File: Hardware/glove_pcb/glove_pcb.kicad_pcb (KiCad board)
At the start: 4 copper layers, 144.6 x 80.7 mm, 124 parts, among them J1 OSTVN02A150, J2 OSTVN02A150, J3 54-00130, J4 0430451000, J5 302-R141, J6 302-R141, J7 61300611121, J8 67997-206HLF, J9 22053061, M1 MountingHole_3.5mm_Pad, M2 MountingHole_3.5mm_Pad, M3 MountingHole_3.5mm_Pad, M4 MountingHole_3.5mm_Pad, U1 AP63205WU, U10 BZA408B, U11 BZA408B, U12 MCP3008, U13 ATmega328PB-A, U14 MCP3008, U15 MCP3008, U16 BM70BLES1FC2-0B04AA, U17 MCP111T-195I/TT, U18 74LVC1T45GW_125, U19 74LVC1T45GW_125, U2 TCR2EF33_LMCT, U3 DRV8876PWPR, U4 DRV8876PWPR, U5 DRV8876PWPR, U6 DRV8876PWPR, U7 DRV8876PWPR, U8 BZA408B, U9 BZA408B

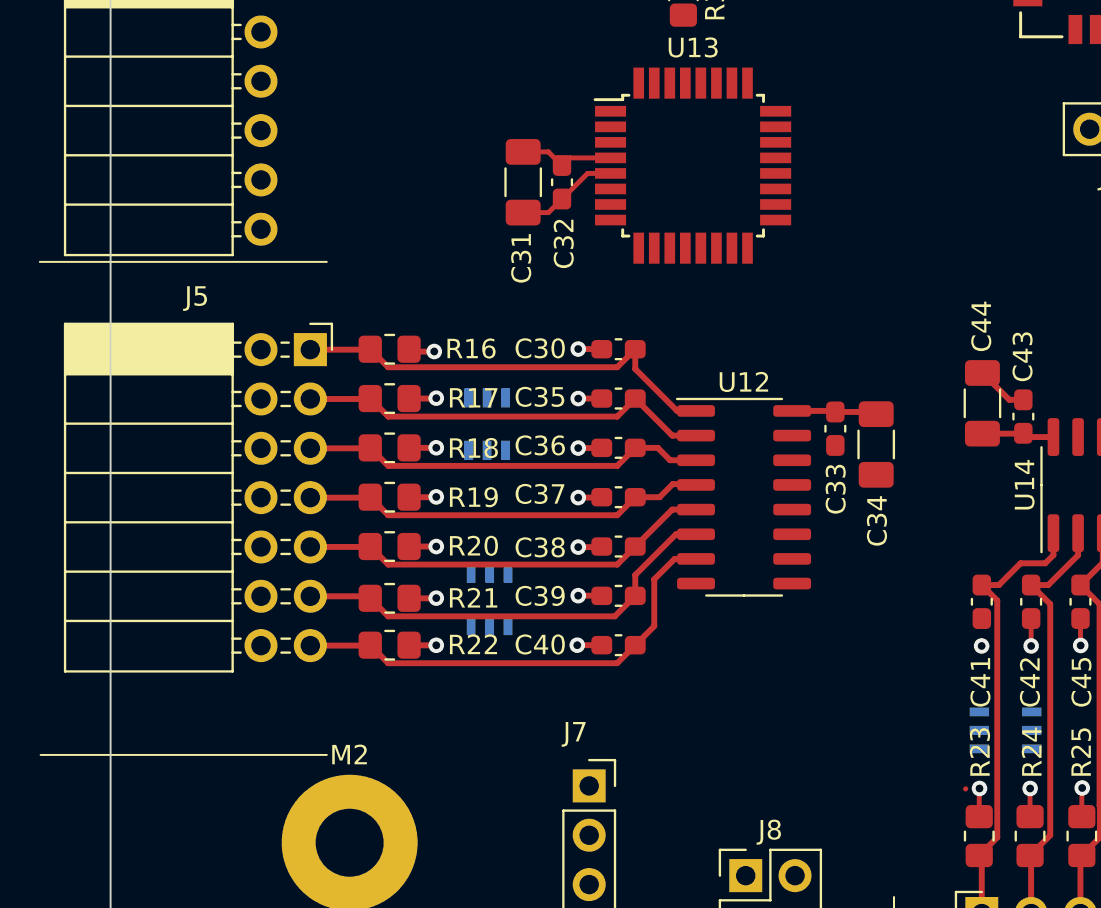
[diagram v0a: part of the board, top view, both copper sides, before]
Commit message: Minor footprint and routing fixes
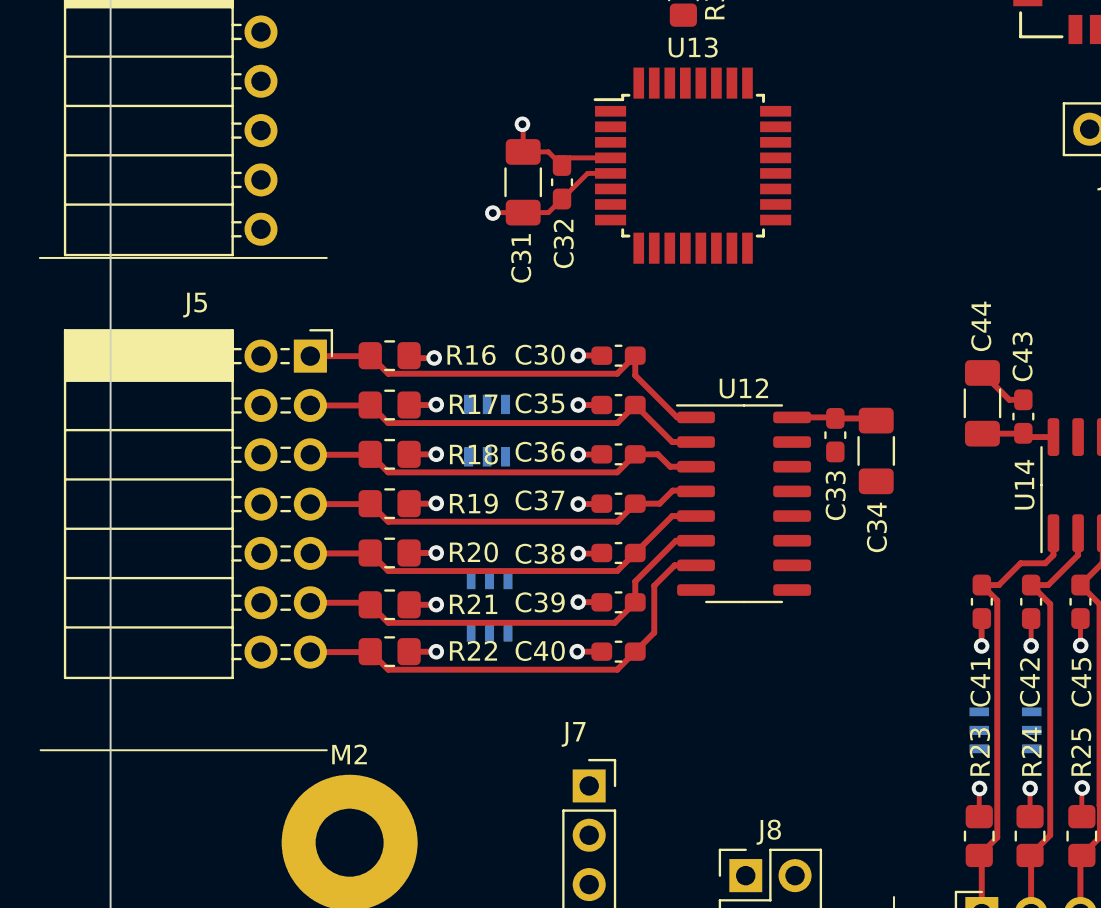
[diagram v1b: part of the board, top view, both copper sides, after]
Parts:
- moved C30 0.33 mm to (94.6, 95.7)
- moved C33 0.33 mm to (105.8, 99.8)
- moved C34 0.33 mm to (107.9, 100.6)
- moved C35 0.33 mm to (94.6, 98.3)
- moved C36 0.33 mm to (94.6, 100.8)
- moved C37 0.33 mm to (94.6, 103.4)
- moved C38 0.33 mm to (94.6, 105.9)
- moved C39 0.33 mm to (94.6, 108.4)
- moved C40 0.33 mm to (94.6, 111.0)
- moved J5 0.33 mm to (78.5, 95.8)
- moved R16 0.33 mm to (82.8, 95.7)
- moved R17 0.33 mm to (82.8, 98.3)
- moved R18 0.33 mm to (82.8, 100.8)
- moved R19 0.33 mm to (82.8, 103.4)
- moved R20 0.33 mm to (82.8, 105.9)
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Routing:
- net GND: track 51.4 -> 54.6 mm, vias 16 -> 17
- net +5V: track 64.8 -> 66.5 mm, vias 17 -> 18

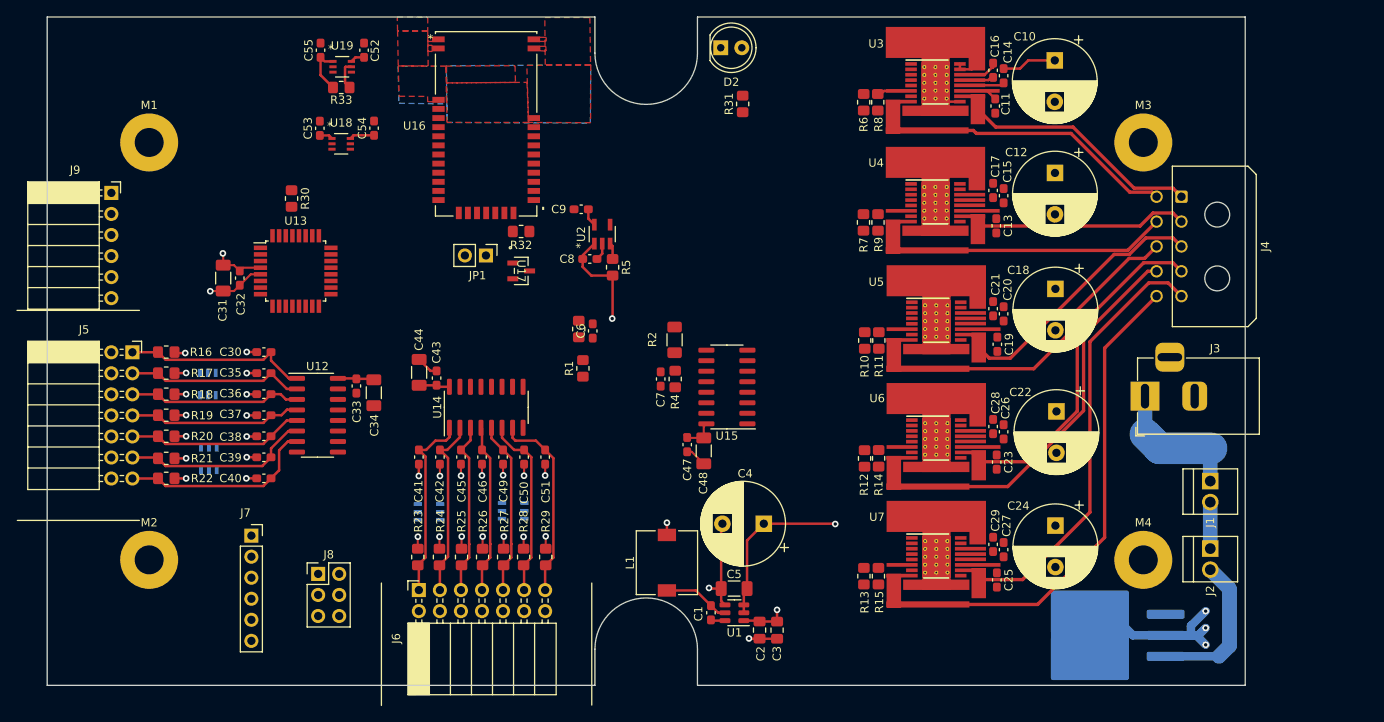
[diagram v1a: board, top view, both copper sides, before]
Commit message: Did the Routing for PCB
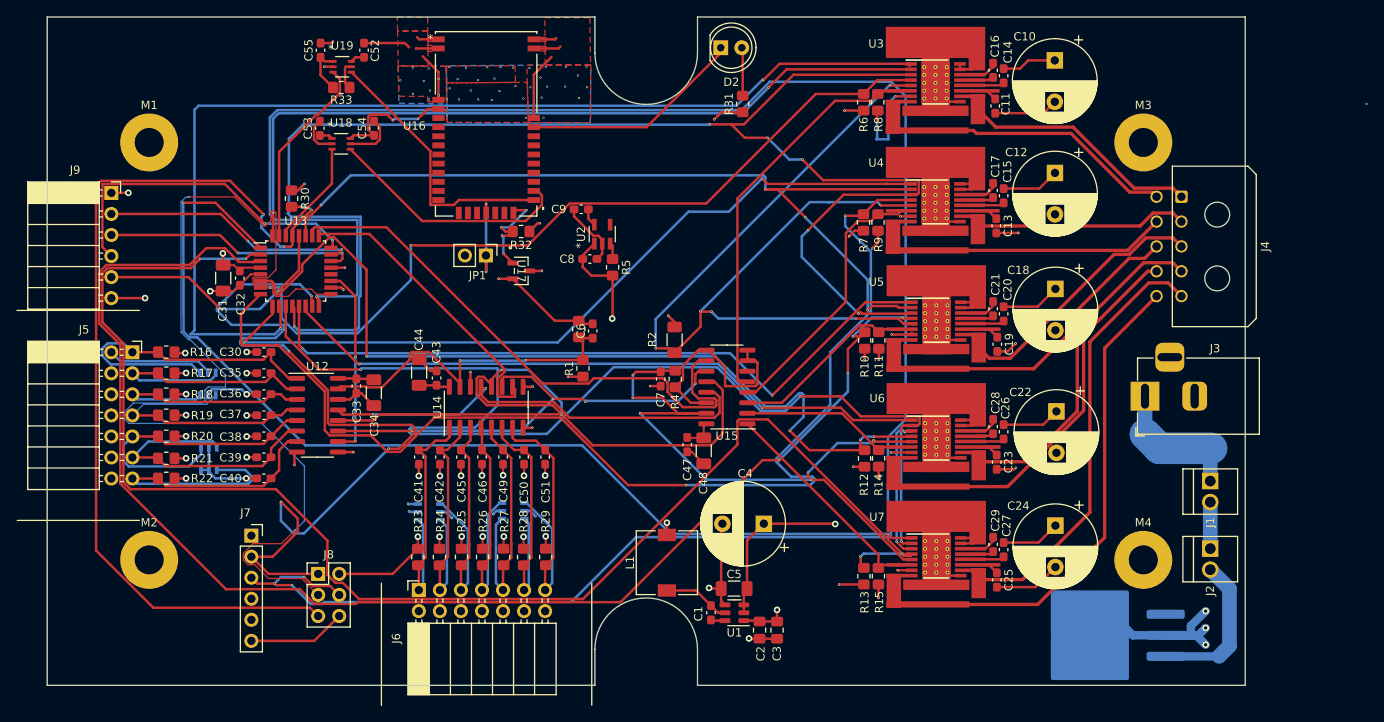
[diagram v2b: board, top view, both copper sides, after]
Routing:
- net MOSI: track 0.00 -> 262.3 mm, vias 0 -> 4
- net GND: track 54.6 -> 294.6 mm, vias 17 -> 48
- net UC_PERIPHERAL_SLEEP_RESET: track 0.00 -> 200.0 mm, vias 0 -> 8
- net MOTOR_AREF: track 0.00 -> 193.4 mm, vias 0 -> 12
- net MOTOR5_FAULT: track 0.00 -> 175.2 mm, vias 0 -> 4
- net MOTOR3_FAULT: track 0.00 -> 170.2 mm, vias 0 -> 4
- net MOTOR2_FAULT: track 0.00 -> 139.8 mm, vias 0 -> 2
- net UC_MOTOR_PH3: track 0.00 -> 135.0 mm, vias 0 -> 4
- net OC0A: track 0.00 -> 130.5 mm, vias 0 -> 2
- net SCK: track 0.00 -> 128.1 mm, vias 0 -> 2
- net OC2B: track 0.00 -> 125.4 mm, vias 0 -> 2
- net MISO1: track 0.00 -> 116.5 mm, vias 0 -> 4
- net RST: track 0.00 -> 110.6 mm, vias 0 -> 4
- net MOTOR4_FAULT: track 0.00 -> 108.4 mm, vias 0 -> 4
- net UC_MOTOR_PH2: track 0.00 -> 105.1 mm, vias 0 -> 4
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
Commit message: Increasing via sizes and minor routing changes
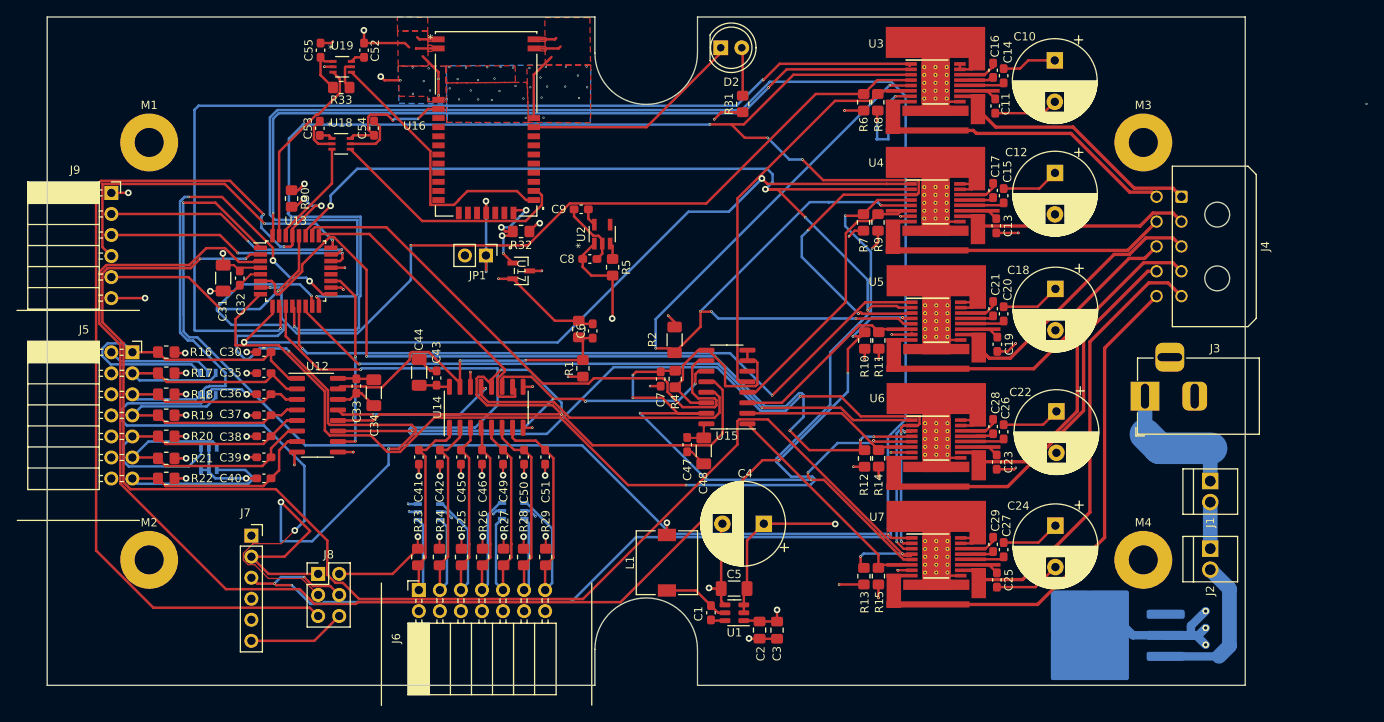
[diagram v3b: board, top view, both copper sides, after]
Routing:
- net SCK: track 128.1 -> 116.5 mm, vias 2 -> 4
- net MISO: track 102.9 -> 111.1 mm
- net GND: track 294.6 -> 299.3 mm, vias 48 -> 87
- net RST: track 110.6 -> 113.7 mm
- net UC_MOTOR_PH2: track 105.1 -> 107.3 mm
- net OC0A: track 130.5 -> 129.2 mm
- net MOTOR2_FAULT: track 139.8 -> 140.9 mm
- net 3V3_TXD: track 32.7 -> 33.6 mm
- net Net-(JP1-A): track 11.4 -> 12.3 mm
- net (no net): vias 39 -> 2
- removed copper zone on F.Cu, net (none)

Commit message: Modified the Vias
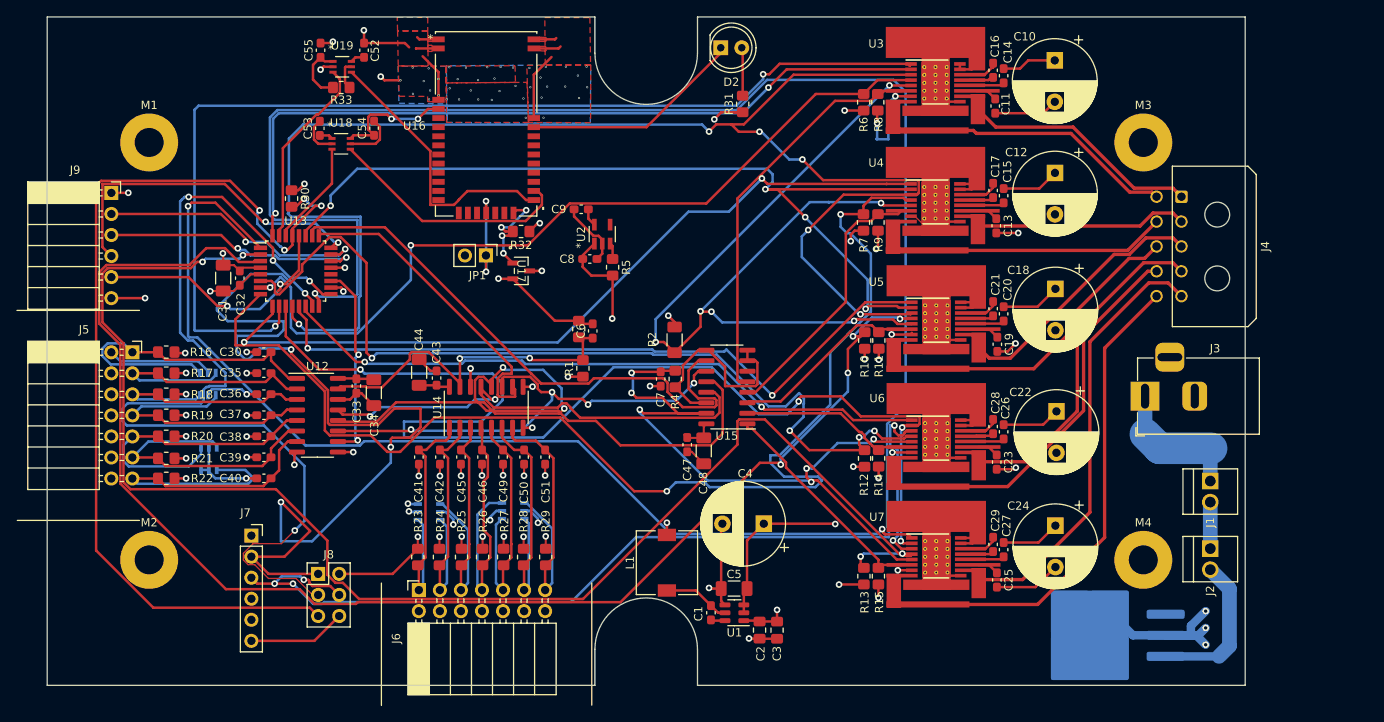
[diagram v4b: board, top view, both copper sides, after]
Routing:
- net GND: track 299.3 -> 306.2 mm, vias 87 -> 86
- net MOTOR2_FAULT: track 140.9 -> 147.4 mm
- net MISO: track 111.1 -> 116.8 mm
- net MISO1: track 116.5 -> 121.1 mm
- net SCK1: track 95.7 -> 99.6 mm
- net UC_PERIPHERAL_SLEEP_RESET: track 200.0 -> 203.9 mm
- net MOSI1: track 87.9 -> 91.3 mm
- net UC_MOTOR_PH3: track 135.0 -> 137.8 mm
- net MOTOR_AREF: track 193.4 -> 196.0 mm
- net +5V: track 99.2 -> 101.7 mm
- net SS_ADC2: track 36.3 -> 38.3 mm
- net MOTOR4_FAULT: track 108.4 -> 110.3 mm
- net MOTOR1_FAULT: track 98.5 -> 100.4 mm
- net POT_RING_3: track 32.1 -> 33.8 mm
- net MOSI: track 262.3 -> 263.7 mm
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
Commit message: Changes from before submission saturday morning
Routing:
- net +12V: track 90.6 -> 136.4 mm, vias 4 -> 9
- net MOSI1: track 91.3 -> 129.1 mm, vias 6 -> 10
- net MISO1: track 121.1 -> 156.8 mm, vias 4 -> 8
- net SCK1: track 99.6 -> 134.9 mm, vias 4 -> 10
- net +5V: track 101.7 -> 132.4 mm, vias 28 -> 33
- net UC_PERIPHERAL_SLEEP_RESET: track 203.9 -> 223.5 mm, vias 8 -> 13
- net MOTOR4_FAULT: track 110.3 -> 119.7 mm
- net GND: track 306.2 -> 302.2 mm, vias 86 -> 93
- net OC1B: track 79.5 -> 83.2 mm
- net MOTOR_AREF: track 196.0 -> 198.9 mm
- net 3V3_TXD: track 33.6 -> 35.6 mm
- net +3.3V: track 26.7 -> 28.7 mm, vias 5 -> 7
- net MOTOR2_FAULT: track 147.4 -> 148.7 mm
- net SCK: track 116.5 -> 117.6 mm
- net SS_IMU: track 31.6 -> 30.7 mm
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- added copper zone on B.Cu, net GND
- removed copper zone on B.Cu, net (none)

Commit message: Changes before/after meeting w Dimitry
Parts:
- moved J7 57.7 mm to (81.8, 61.3), turned to 90 degrees
- moved J8 56.3 mm to (87.9, 67.8)
- moved C3 3.64 mm to (154.1, 132.0), turned to 180 degrees
- moved U8 0.85 mm to (88.0, 98.8)
- moved C2 0.69 mm to (154.2, 129.9), turned to 180 degrees
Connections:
- U15 pad 1: MOTOR1_ISEN -> MOTOR5_ISEN
- U15 pad 2: MOTOR2_ISEN -> MOTOR4_ISEN
- U15 pad 4: MOTOR4_ISEN -> MOTOR2_ISEN
- U15 pad 5: MOTOR5_ISEN -> MOTOR1_ISEN
- U15 pad 6: unconnected-(U15-CH5-Pad6) -> GND
- U8 pad 1: POT_THUMB_1 -> POT_THUMB_2
- U8 pad 3: POT_THUMB_2 -> POT_THUMB_1
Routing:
- net MOSI: track 263.7 -> 0.00 mm, vias 4 -> 0
- net SCK: track 117.6 -> 0.00 mm, vias 4 -> 0
- net MISO: track 117.0 -> 0.00 mm, vias 4 -> 0
- net RST: track 114.1 -> 9.86 mm, vias 4 -> 2
- net GND: track 302.2 -> 262.9 mm, vias 93 -> 94
- net +5V: track 132.4 -> 119.5 mm, vias 33 -> 32
- net +12V: track 136.4 -> 146.7 mm, vias 9 -> 11
- net SCK1: track 134.9 -> 140.6 mm
- net OC0A: track 128.7 -> 123.2 mm
- net POT_THUMB_1: track 40.4 -> 35.8 mm
- net Net-(JP1-A): track 12.3 -> 8.32 mm, vias 2 -> 1
- net POT_THUMB_2: track 33.0 -> 30.5 mm
- net MOTOR5_FAULT: track 175.4 -> 174.1 mm
- net MOTOR1_ISEN: track 48.7 -> 47.8 mm
- net OC2B: track 125.7 -> 124.9 mm
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
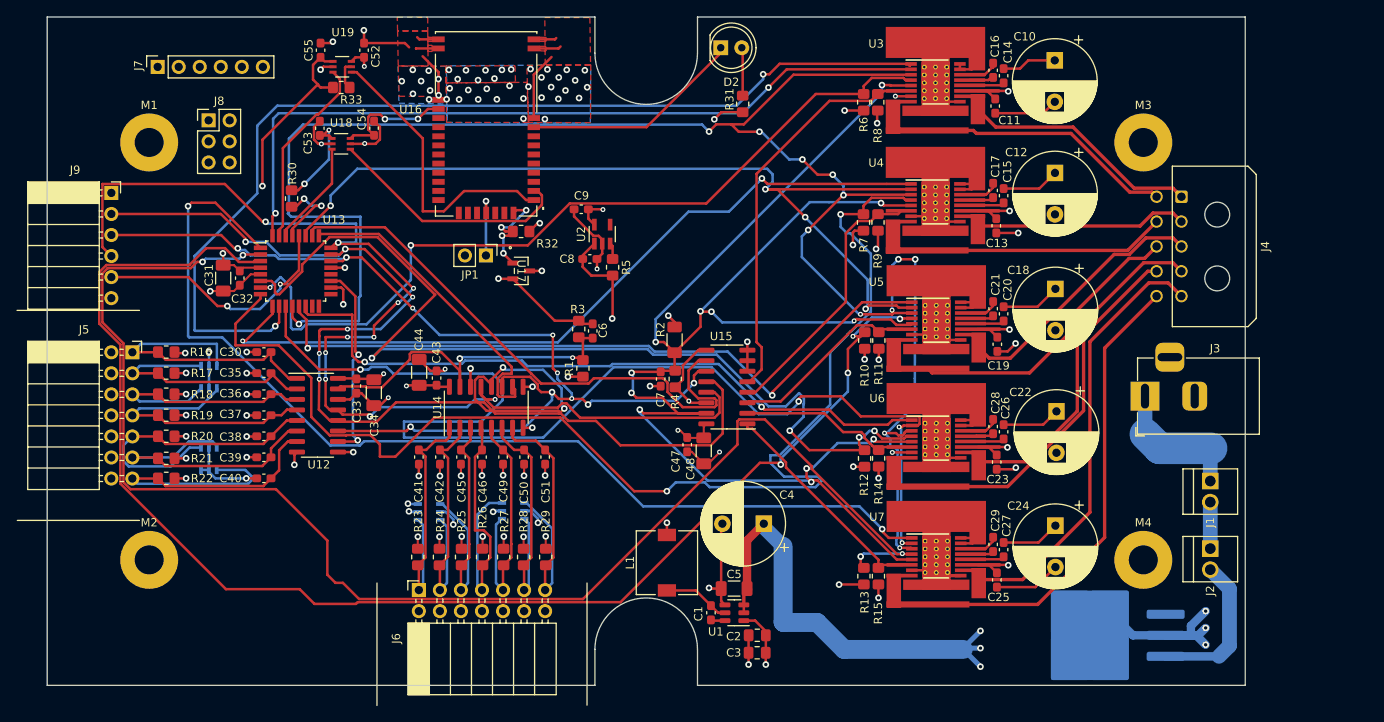
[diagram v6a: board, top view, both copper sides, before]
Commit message: Fixed some of the clearance as well as some routing issues
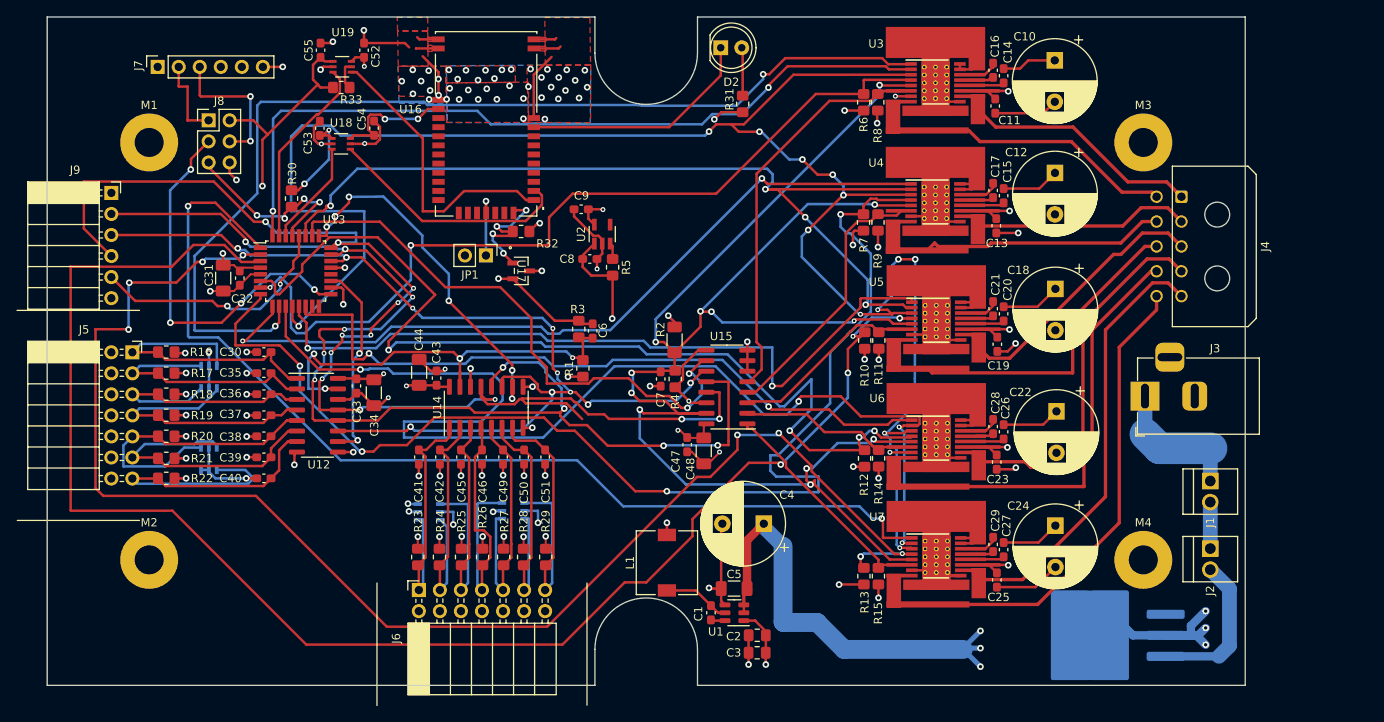
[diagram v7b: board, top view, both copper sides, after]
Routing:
- net SCK: track 0.00 -> 47.0 mm, vias 0 -> 4
- net MOSI: track 0.00 -> 17.6 mm, vias 0 -> 2
- net MOTOR3_FAULT: track 170.8 -> 187.1 mm
- net RST: track 9.86 -> 23.7 mm, vias 2 -> 4
- net SCK1: track 140.6 -> 152.5 mm, vias 10 -> 12
- net MISO1: track 156.8 -> 145.9 mm, vias 8 -> 10
- net POT_AREF: track 43.3 -> 53.5 mm, vias 2 -> 4
- net MISO: track 0.00 -> 10.1 mm
- net GND: track 262.9 -> 269.0 mm, vias 94 -> 96
- net SS_ADC2: track 38.3 -> 43.8 mm, vias 0 -> 7
- net +5V: track 119.5 -> 124.8 mm
- net MOTOR4_OUT1: track 43.7 -> 48.8 mm
- net MOTOR4_OUT2: track 40.8 -> 45.4 mm
- net OC1A: track 85.9 -> 90.0 mm
- net Net-(U16-RST_N): track 12.7 -> 15.7 mm
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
